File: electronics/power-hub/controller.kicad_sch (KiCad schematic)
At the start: 56 parts, among them J6 USB, SW1 RESET, SW2 BOOT, U2 LMR51635YDDCR, U3 AP2112K-3.3TRG1, U4 ESP32-S3-MINI-1-N8, U5 USBLC6-2SC6, U6 TCAN1462V

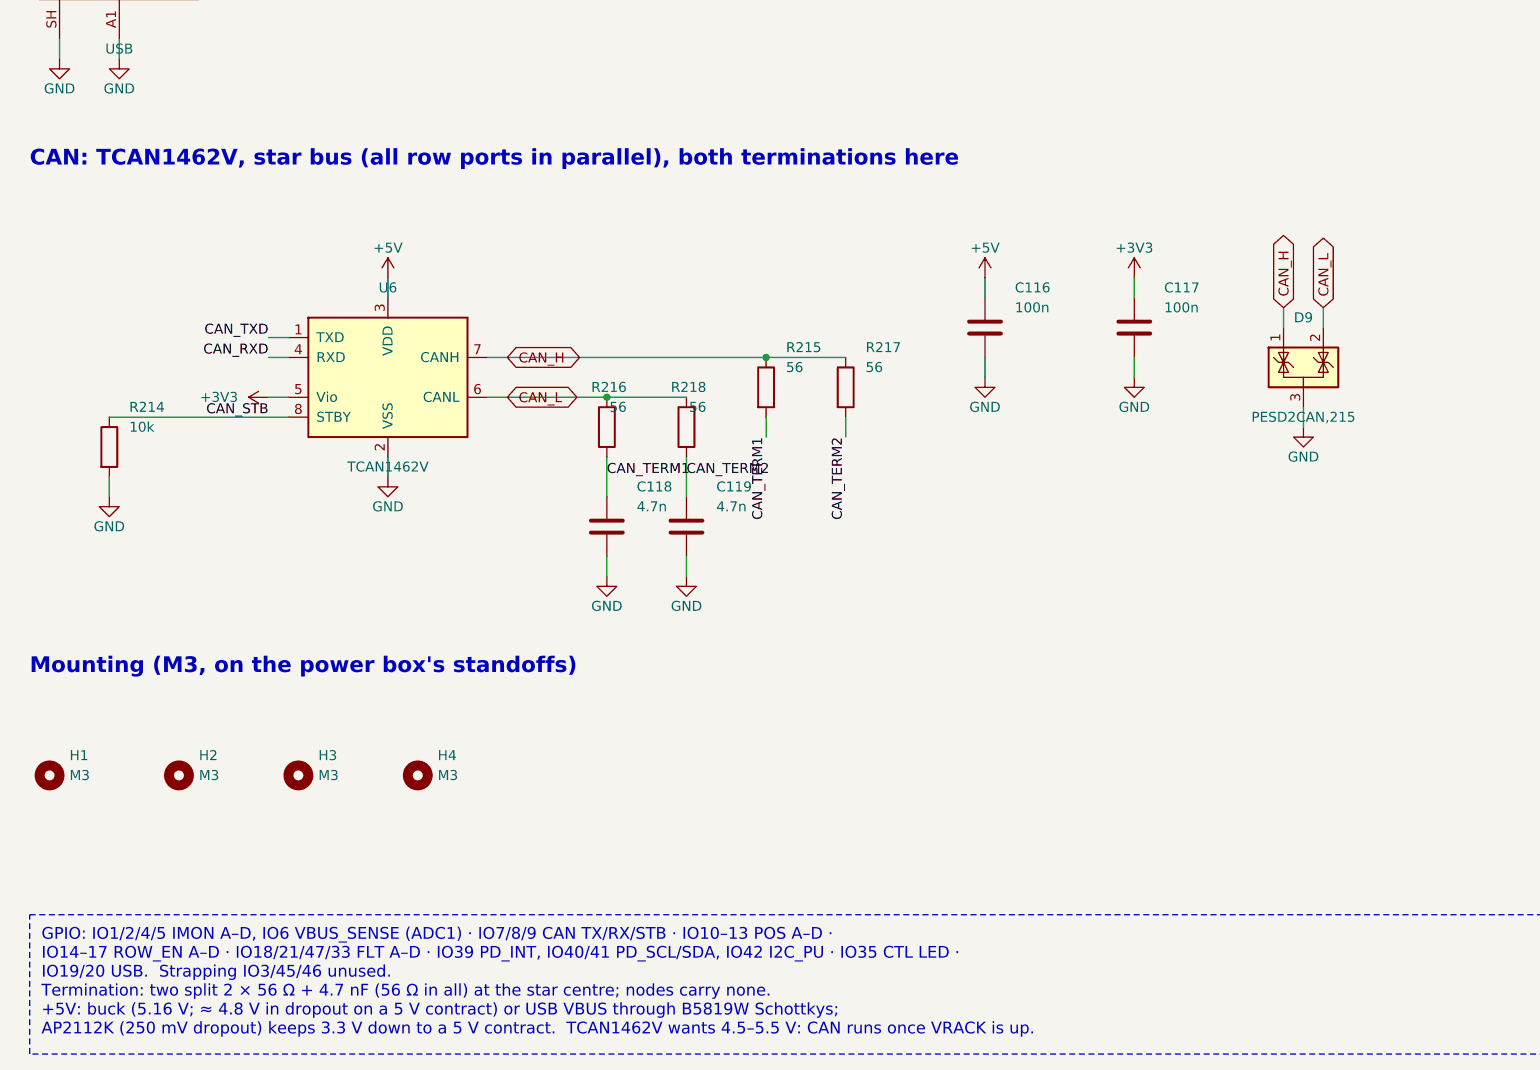
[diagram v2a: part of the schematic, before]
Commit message: CAN transceiver: the TJA1462AT on the hub and the node
The TCAN1462V (C7399456) had no LCSC stock on 2026-10-18 and 19, and
JLC's quote of the hub asked for another part.  The user chose NXP's
TJA1462AT/0Z (C3234095, 10 500 in stock) for both boards (hub U6, node
U11): the same SOIC-8 pinout (VIO on pin 5, STB on pin 8), signal
improvement kept, bus pins -36/+40 V instead of ±58 V.  The TCAN1462V
and the TCAN1044AV stay the alternates.

Both boards regenerated and the same Freerouting sessions re-imported
(tracks and vias unchanged): ERC 0, DRC 0 errors (the hub's known C8
silkscreen warning), 0 unconnected, parity 0, JLC READY.  The CPL keeps
its 270° correction (C3234095 was already in build_board.py).

Docs: can.md, electronics.md, firmware comments and pin tables,
bom/sourcing.md, which also notes that JLC unticks the USB4105 (hard to
process, $0.03 a piece): tick it again at every order.

Co-Authored-By: Claude Opus 5.5 <noreply@anthropic.com>
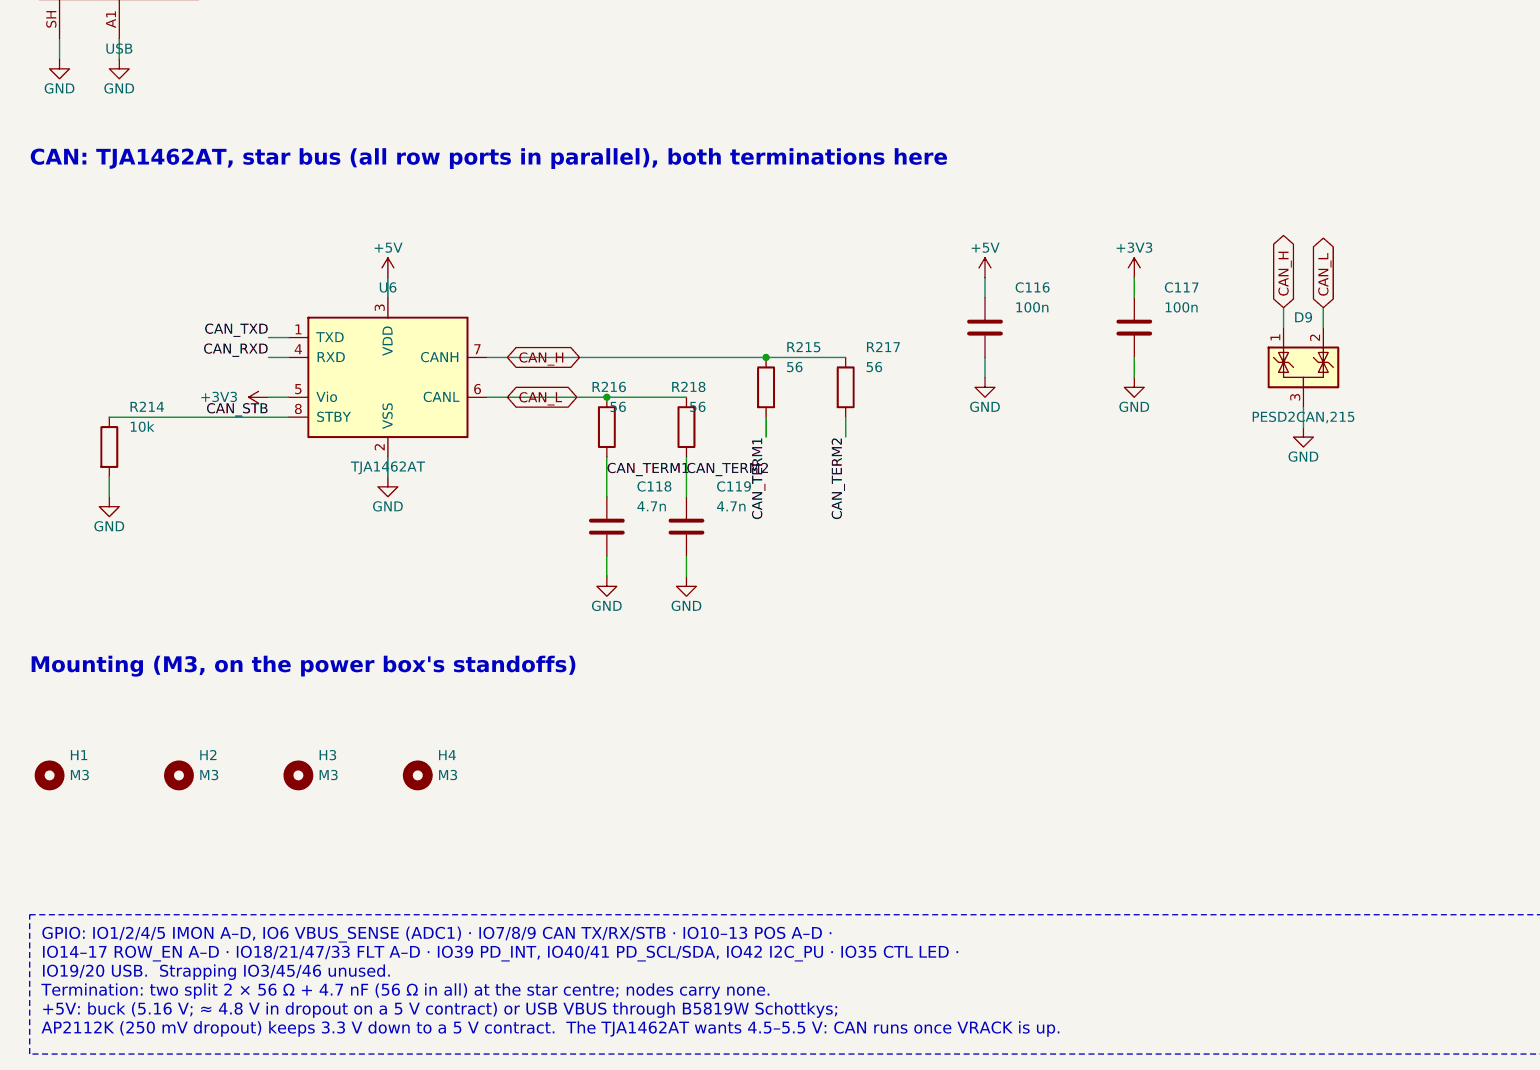
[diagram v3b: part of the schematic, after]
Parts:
- U6: value TCAN1462V -> TJA1462AT; Alternative LCSC stock was 0 on 2026-10-18. Same pinout: TCAN1044AVDRQ1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 -> Same pinout: TI TCAN1462VDRQ1 (C7399456, SIC, bus pins ±58 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; LCSC C7399456 -> C3234095; MPN TCAN1462VDRQ1 -> TJA1462AT/0Z; Manufacturer Texas Instruments -> NXP Semiconductors
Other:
- note added: "CAN: TJA1462AT, star bus (all row ports in parallel), both terminations here"
- note removed: "CAN: TCAN1462V, star bus (all row ports in parallel), both terminations here"
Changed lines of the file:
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@@
 		)
 	)
-	(text "CAN: TCAN1462V, star bus (all row ports in parallel), both terminations here"
+	(text "CAN: TJA1462AT, star bus (all row ports in parallel), both terminations here"
 		(exclude_from_sim no)
 		(at 20.32 320.04 0)
@@
 			)
 		)
-		(property "Value" "TCAN1462V"
+		(property "Value" "TJA1462AT"
 			(at 66.04 358.14 0)
 			(effects
@@
 			)
 		)
-		(property "Datasheet" "https://www.ti.com/lit/ds/symlink/tcan1462-q1.pdf"
+		(property "Datasheet" "https://www.nxp.com/docs/en/data-sheet/TJA1462.pdf"
 			(at 66.04 346.71 0)
 			(effects
@@
 			)
 		)
-		(property "Description" "CAN FD SIC transceiver, VCC 5 V, VIO 1.7–5.5 V, bus pins ±58 V (MCP2562 pinout)"
+		(property "Description" "CAN FD SIC transceiver, VCC 5 V, VIO 2.95–5.5 V, bus pins −36/+40 V (MCP2562 pinout)"
 			(at 66.04 346.71 0)
 			(effects
@@
 			)
 		)
-		(property "MPN" "TCAN1462VDRQ1"
+		(property "MPN" "TJA1462AT/0Z"
 			(at 66.04 346.71 0)
 			(effects
@@
 			)
 		)
-		(property "Manufacturer" "Texas Instruments"
+		(property "Manufacturer" "NXP Semiconductors"
 			(at 66.04 346.71 0)
 			(effects
@@
 			)
 		)
-		(property "LCSC" "C7399456"
+		(property "LCSC" "C3234095"
 			(at 66.04 346.71 0)
 			(effects
@@
 			)
 		)
-		(property "Alternative" "LCSC stock was 0 on 2026-10-18.  Same pinout: TCAN1044AVDRQ1 (C3234993, no SIC, ±58 V) or NXP TJA1462AT/0Z (C3234095, SIC, VIO 2.95–5.5 V, bus pins −36/+40 V)"
+		(property "Alternative" "Same pinout: TI TCAN1462VDRQ1 (C7399456, SIC, bus pins ±58 V; LCSC stock 0 on 2026-10-18 and 19) or TCAN1044AVDRQ1 (C3234993, no SIC, ±58 V)"
 			(at 66.04 346.71 0)
 			(effects
@@
 		)
 	)
-	(text_box "GPIO: IO1/2/4/5 IMON A–D, IO6 VBUS_SENSE (ADC1) · IO7/8/9 CAN TX/RX/STB · IO10–13 POS A–D ·\n  IO14–17 ROW_EN A–D · IO18/21/47/33 FLT A–D · IO39 PD_INT, IO40/41 PD_SCL/SDA, IO42 I2C_PU · IO35 CTL LED ·\n  IO19/20 USB.  Strapping IO3/45/46 unused.\nTermination: two split 2 × 56 Ω + 4.7 nF (56 Ω in all) at the star centre; nodes carry none.\n+5V: buck (5.16 V; ≈ 4.8 V in dropout on a 5 V contract) or USB VBUS through B5819W Schottkys;\n  AP2112K (250 mV dropout) keeps 3.3 V down to a 5 V contract.  TCAN1462V wants 4.5–5.5 V: CAN runs once VRACK is up."
+	(text_box "GPIO: IO1/2/4/5 IMON A–D, IO6 VBUS_SENSE (ADC1) · IO7/8/9 CAN TX/RX/STB · IO10–13 POS A–D ·\n  IO14–17 ROW_EN A–D · IO18/21/47/33 FLT A–D · IO39 PD_INT, IO40/41 PD_SCL/SDA, IO42 I2C_PU · IO35 CTL LED ·\n  IO19/20 USB.  Strapping IO3/45/46 unused.\nTermination: two split 2 × 56 Ω + 4.7 nF (56 Ω in all) at the star centre; nodes carry none.\n+5V: buck (5.16 V; ≈ 4.8 V in dropout on a 5 V contract) or USB VBUS through B5819W Schottkys;\n  AP2112K (250 mV dropout) keeps 3.3 V down to a 5 V contract.  The TJA1462AT wants 4.5–5.5 V: CAN runs once VRACK is up."
 		(exclude_from_sim no)
 		(at 20.32 415.29 0)

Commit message: Power hub: lead-free HASL and six part types fewer, ≈ $22 off
The user found the hub dear ($242.52 quoted).  JLC's calculator
(2026-10-19, 5 boards, 4 layers) shows where it goes: ENIG $18.00
against lead-free HASL $5.30, and the $25 engineering fee comes from the
length (86 x 100 mm with the rails falls under the 4-layer offer).

- Finish: lead-free HASL, as the node.  It was ENIG for the MINI-1's LGA
  pads; JLC X-rays the module either way.  -$12.70.
- Six resistor values merged onto values the board already has (no
  footprint or track moves): FB 100k/18k (5.24 V, as the node), EN
  39k/18k (on at 3.9 V), PD INT 10k/18k (3.2 V), I2C pull-ups 5.1k.
  Six fewer part types at $1.55 in Standard PCBA's feeders: -$9.30.

Same Freerouting session re-imported (1241 segments, 593 vias): ERC 0,
DRC only the known C8 silkscreen warning, 0 unconnected, parity 0.
tools/bom.py applies both to the quote as adjustments: ≈ $220.52.

Co-Authored-By: Claude Opus 5.5 <noreply@anthropic.com>
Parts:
- R205: value 100k -> 39k; LCSC C25803 -> C23153; MPN 0603WAF1003T5E -> 0603WAF3902T5E
- R206: value 47k -> 18k; LCSC C25819 -> C25810; MPN 0603WAF4702T5E -> 0603WAF1802T5E
- R207: value 120k -> 100k; LCSC C25808 -> C25803; MPN 0603WAF1203T5E -> 0603WAF1003T5E
- R208: value 22k -> 18k; LCSC C31850 -> C25810; MPN 0603WAF2202T5E -> 0603WAF1802T5E
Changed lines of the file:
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@@
 			)
 		)
-		(property "Value" "100k"
+		(property "Value" "39k"
 			(at 33.02 45.72 0)
 			(effects
@@
 			)
 		)
-		(property "Description" "Resistor 100k 0603"
+		(property "Description" "Resistor 39k 0603"
 			(at 30.48 48.26 0)
 			(effects
@@
 			)
 		)
-		(property "LCSC" "C25803"
+		(property "LCSC" "C23153"
 			(at 30.48 48.26 0)
 			(effects
@@
 			)
 		)
-		(property "MPN" "0603WAF1003T5E"
+		(property "MPN" "0603WAF3902T5E"
 			(at 30.48 48.26 0)
 			(effects
@@
 			)
 		)
-		(property "Value" "47k"
+		(property "Value" "18k"
 			(at 73.66 50.8 0)
 			(effects
@@
 			)
 		)
-		(property "Description" "Resistor 47k 0603"
+		(property "Description" "Resistor 18k 0603"
 			(at 71.12 53.34 0)
 			(effects
@@
 			)
 		)
-		(property "LCSC" "C25819"
+		(property "LCSC" "C25810"
 			(at 71.12 53.34 0)
 			(effects
@@
 			)
 		)
-		(property "MPN" "0603WAF4702T5E"
+		(property "MPN" "0603WAF1802T5E"
 			(at 71.12 53.34 0)
 			(effects
@@
 			)
 		)
-		(property "Value" "120k"
+		(property "Value" "100k"
 			(at 133.35 50.8 0)
 			(effects
@@
 			)
 		)
-		(property "Description" "Resistor 120k 0603"
+		(property "Description" "Resistor 100k 0603"
 			(at 130.81 53.34 0)
 			(effects
@@
 			)
 		)
-		(property "LCSC" "C25808"
+		(property "LCSC" "C25803"
 			(at 130.81 53.34 0)
 			(effects
@@
 			)
 		)
-		(property "MPN" "0603WAF1203T5E"
+		(property "MPN" "0603WAF1003T5E"
 			(at 130.81 53.34 0)
 			(effects
@@
 			)
 		)
-		(property "Value" "22k"
+		(property "Value" "18k"
 			(at 143.51 50.8 0)
 			(effects
@@
 			)
 		)
-		(property "Description" "Resistor 22k 0603"
+		(property "Description" "Resistor 18k 0603"
 			(at 140.97 53.34 0)
 			(effects
@@
 			)
 		)
-		(property "LCSC" "C31850"
+		(property "LCSC" "C25810"
 			(at 140.97 53.34 0)
 			(effects
@@
 			)
 		)
-		(property "MPN" "0603WAF2202T5E"
+		(property "MPN" "0603WAF1802T5E"
 			(at 140.97 53.34 0)
 			(effects
@@
 		)
 	)
-	(text_box "GPIO: IO1/2/4/5 IMON A–D, IO6 VBUS_SENSE (ADC1) · IO7/8/9 CAN TX/RX/STB · IO10–13 POS A–D ·\n  IO14–17 ROW_EN A–D · IO18/21/47/33 FLT A–D · IO39 PD_INT, IO40/41 PD_SCL/SDA, IO42 I2C_PU · IO35 CTL LED ·\n  IO19/20 USB.  Strapping IO3/45/46 unused.\nTermination: two split 2 × 56 Ω + 4.7 nF (56 Ω in all) at the star centre; nodes carry none.\n+5V: buck (5.16 V; ≈ 4.8 V in dropout on a 5 V contract) or USB VBUS through B5819W Schottkys;\n  AP2112K (250 mV dropout) keeps 3.3 V down to a 5 V contract.  The TJA1462AT wants 4.5–5.5 V: CAN runs once VRACK is up."
+	(text_box "GPIO: IO1/2/4/5 IMON A–D, IO6 VBUS_SENSE (ADC1) · IO7/8/9 CAN TX/RX/STB · IO10–13 POS A–D ·\n  IO14–17 ROW_EN A–D · IO18/21/47/33 FLT A–D · IO39 PD_INT, IO40/41 PD_SCL/SDA, IO42 I2C_PU · IO35 CTL LED ·\n  IO19/20 USB.  Strapping IO3/45/46 unused.\nTermination: two split 2 × 56 Ω + 4.7 nF (56 Ω in all) at the star centre; nodes carry none.\n+5V: buck (5.24 V; ≈ 4.8 V in dropout on a 5 V contract) or USB VBUS through B5819W Schottkys;\n  AP2112K (250 mV dropout) keeps 3.3 V down to a 5 V contract.  The TJA1462AT wants 4.5–5.5 V: CAN runs once VRACK is up."
 		(exclude_from_sim no)
 		(at 20.32 415.29 0)

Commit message: Power hub: 38 part types (48 at the quote), the list by function
The user asked why the hub has so many part types.  Four more values
merged onto parts the board already has, no footprint or track moved:
every front LED on 1k (1.2-1.4 mA; 330 and 680 gone), the CAN split
caps on the IMON filters' 10 nF (4.7 nF gone), the LDO's input cap on
the eFuses' 1 µF 0805 (10 µF 0805 gone; the buck's 3 x 22 µF sit just
before D4).  With the six of e7ecf78: 48 -> 38 types, -$15.50 of
Standard PCBA feeders; the order is ≈ $214.32 against $242.52 quoted.

docs/electronics.md lists the types per block (five jobs; the four
eFuse rows repeat the same parts) and what two rows instead of four
would remove: no type, 36 parts a board, ≈ $10 for two boards.

Same Freerouting session (1241 segments, 593 vias): ERC 0, DRC only the
known C8 silkscreen warning, 0 unconnected, parity 0.

Co-Authored-By: Claude Opus 5.5 <noreply@anthropic.com>
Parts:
- C111: value 10u -> 1u; LCSC C15850 -> C28323; MPN CL21A106KAYNNNE -> CL21B105KBFNNNE
- C118, C119: value 4.7n -> 10n; LCSC C53987 -> C57112; MPN 0603B472K500NT -> 0603B103K500NT
- R211: value 330 -> 1k; LCSC C23138 -> C21190; MPN 0603WAF3300T5E -> 0603WAF1001T5E
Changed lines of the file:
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@@
 			)
 		)
-		(property "Value" "10u"
+		(property "Value" "1u"
 			(at 184.15 102.87 0)
 			(effects
@@
 			)
 		)
-		(property "Description" "Capacitor 10u 0805"
+		(property "Description" "Capacitor 1u 0805"
 			(at 180.34 105.41 0)
 			(effects
@@
 			)
 		)
-		(property "LCSC" "C15850"
+		(property "LCSC" "C28323"
 			(at 180.34 105.41 0)
 			(effects
@@
 			)
 		)
-		(property "MPN" "CL21A106KAYNNNE"
+		(property "MPN" "CL21B105KBFNNNE"
 			(at 180.34 105.41 0)
 			(effects
@@
 			)
 		)
-		(property "Value" "330"
+		(property "Value" "1k"
 			(at 187.96 171.45 0)
 			(effects
@@
 			)
 		)
-		(property "Description" "Resistor 330 0603"
+		(property "Description" "Resistor 1k 0603"
 			(at 185.42 173.99 0)
 			(effects
@@
 			)
 		)
-		(property "LCSC" "C23138"
+		(property "LCSC" "C21190"
 			(at 185.42 173.99 0)
 			(effects
@@
 			)
 		)
-		(property "MPN" "0603WAF3300T5E"
+		(property "MPN" "0603WAF1001T5E"
 			(at 185.42 173.99 0)
 			(effects
@@
 			)
 		)
-		(property "Value" "4.7n"
+		(property "Value" "10n"
 			(at 97.79 363.22 0)
 			(effects
@@
 			)
 		)
-		(property "Description" "Capacitor 4.7n 0603"
+		(property "Description" "Capacitor 10n 0603"
 			(at 93.98 365.76 0)
 			(effects
@@
 			)
 		)
-		(property "LCSC" "C53987"
+		(property "LCSC" "C57112"
 			(at 93.98 365.76 0)
 			(effects
@@
 			)
 		)
-		(property "MPN" "0603B472K500NT"
+		(property "MPN" "0603B103K500NT"
 			(at 93.98 365.76 0)
 			(effects
@@
 			)
 		)
-		(property "Value" "4.7n"
+		(property "Value" "10n"
 			(at 107.95 363.22 0)
 			(effects
@@
 			)
 		)
-		(property "Description" "Capacitor 4.7n 0603"
+		(property "Description" "Capacitor 10n 0603"
 			(at 104.14 365.76 0)
 			(effects
@@
 			)
 		)
-		(property "LCSC" "C53987"
+		(property "LCSC" "C57112"
 			(at 104.14 365.76 0)
 			(effects
@@
 			)
 		)
-		(property "MPN" "0603B472K500NT"
+		(property "MPN" "0603B103K500NT"
 			(at 104.14 365.76 0)
 			(effects

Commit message: Hub 37 and node 38 part types: more values merged
From the JLC cost session's list (it does the analysis, this session
edits the boards).  No footprint or track moves; both boards regenerated
on their Freerouting sessions (node 996/386, hub 1241/593 segments/vias),
ERC 0, DRC 0 errors (the hub's known C8 silkscreen warning), parity 0.

- Hub: the IMON filters and the CAN split caps on the dVdT caps' 22 nF
  (IMON RC 22 µs; the split cap only filters common mode): 38 -> 37 types,
  -$17.05 of feeders against the quote, order ≈ $212.77.
- Node: buck EN 100k/10k (same 13.5 V / 10.8 V), PC_DET 10k/18k (3.2 V),
  I²C pull-ups 5.1k, AUX VREF 33 Ω: 42 -> 38 types, estimate ≈ $322.77.

Docs: electronics.md (the hub's types per block, the node's estimate),
can.md, firmware pin tables.

Co-Authored-By: Claude Opus 5.5 <noreply@anthropic.com>
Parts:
- C118, C119: value 10n -> 22n; LCSC C57112 -> C21122; MPN 0603B103K500NT -> CL10B223KB8NNNC; Manufacturer FH (Guangdong Fenghua Advanced Tech) -> Samsung Electro-Mechanics
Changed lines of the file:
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@@
 			)
 		)
-		(property "Value" "10n"
+		(property "Value" "22n"
 			(at 97.79 363.22 0)
 			(effects
@@
 			)
 		)
-		(property "Description" "Capacitor 10n 0603"
-			(at 93.98 365.76 0)
-			(effects
-				(font
-					(size 1.27 1.27)
-				)
-				(hide yes)
-			)
-		)
-		(property "LCSC" "C57112"
-			(at 93.98 365.76 0)
-			(effects
-				(font
-					(size 1.27 1.27)
-				)
-				(hide yes)
-			)
-		)
-		(property "MPN" "0603B103K500NT"
-			(at 93.98 365.76 0)
-			(effects
-				(font
-					(size 1.27 1.27)
-				)
-				(hide yes)
-			)
-		)
-		(property "Manufacturer" "FH (Guangdong Fenghua Advanced Tech)"
+		(property "Description" "Capacitor 22n 0603"
+			(at 93.98 365.76 0)
+			(effects
+				(font
+					(size 1.27 1.27)
+				)
+				(hide yes)
+			)
+		)
+		(property "LCSC" "C21122"
+			(at 93.98 365.76 0)
+			(effects
+				(font
+					(size 1.27 1.27)
+				)
+				(hide yes)
+			)
+		)
+		(property "MPN" "CL10B223KB8NNNC"
+			(at 93.98 365.76 0)
+			(effects
+				(font
+					(size 1.27 1.27)
+				)
+				(hide yes)
+			)
+		)
+		(property "Manufacturer" "Samsung Electro-Mechanics"
 			(at 93.98 365.76 0)
 			(effects
@@
 			)
 		)
-		(property "Value" "10n"
+		(property "Value" "22n"
 			(at 107.95 363.22 0)
 			(effects
@@
 			)
 		)
-		(property "Description" "Capacitor 10n 0603"
-			(at 104.14 365.76 0)
-			(effects
-				(font
-					(size 1.27 1.27)
-				)
-				(hide yes)
-			)
-		)
-		(property "LCSC" "C57112"
-			(at 104.14 365.76 0)
-			(effects
-				(font
-					(size 1.27 1.27)
-				)
-				(hide yes)
-			)
-		)
-		(property "MPN" "0603B103K500NT"
-			(at 104.14 365.76 0)
-			(effects
-				(font
-					(size 1.27 1.27)
-				)
-				(hide yes)
-			)
-		)
-		(property "Manufacturer" "FH (Guangdong Fenghua Advanced Tech)"
-			(at 104.14 365.76 0)
-			(effects
+		(property "Description" "Capacitor 22n 0603"
+			(at 104.14 365.76 0)
+			(effects
+				(font
+					(size 1.27 1.27)
+				)
+				(hide yes)
+			)
+		)
+		(property "LCSC" "C21122"
+			(at 104.14 365.76 0)
+			(effects
+				(font
+					(size 1.27 1.27)
+				)
+				(hide yes)
+			)
+		)
+		(property "MPN" "CL10B223KB8NNNC"
+			(at 104.14 365.76 0)
+			(effects
+				(font
+					(size 1.27 1.27)
+				)
+				(hide yes)
+			)
+		)
+		(property "Manufacturer" "Samsung Electro-Mechanics"
+			(at 104.14 365.76 0)
+			(effects
